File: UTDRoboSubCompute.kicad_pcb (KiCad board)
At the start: 4 copper layers, 100 x 100.1 mm, 52 parts, among them IC1 TPD4E05U06QDQARQ1, IC2 TPD4E05U06QDQARQ1, J1 Disable Bluetooth/Wifi, J10 HEADER-3X04, J11 HEADER-3X04, J12 HEADER-3X04, J13 Conn_02x20_Odd_Even, J14 GSB3116344KHHR, J15 GSB3116344KHHR, J16 TF38-22S-0.5SV_830_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

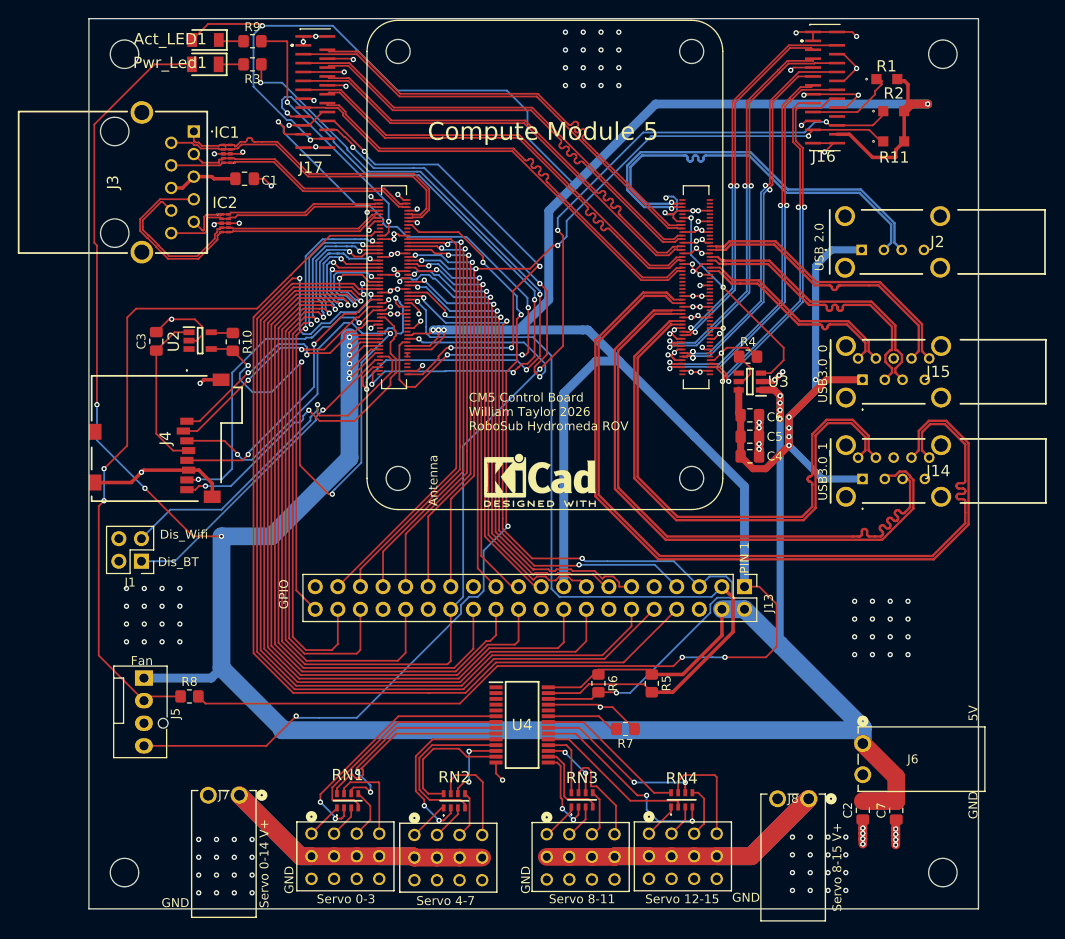
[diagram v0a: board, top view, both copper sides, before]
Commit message: Better trace spacing, JLCPCB compliant & misc fixes
 - Added JLCPCB rules file
 - Made design JLCPCB compliant
 - updated README.md with additional details about diff and non-diff trace routing
 - updated images in README.md
 - updated clearance specs for signaling lines to 3*W
 - flipped GPIO header and reflected spacing changes in routing
 - Fixed Servo Address register floating pins issue
 - Fixed 3.3v input on SD power IC non-connection
 - rerouted servo PWM lines for better spacing
 - rerouted SD card data lines for better spacing, and clearer routes
 - Switched Servo Power Traces to fills in order to allow for multi-layer connections
 - added extra pads for bulk capacitors
 - added more descriptive silkscreens
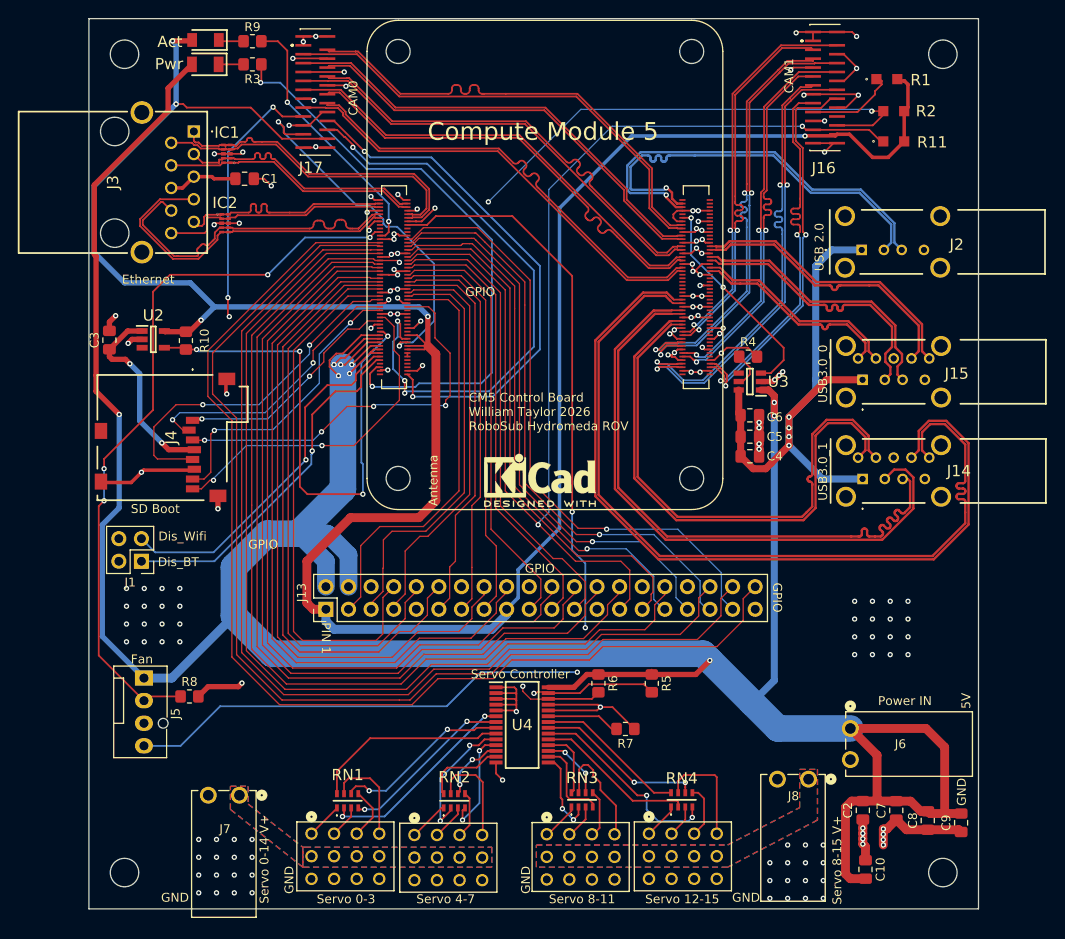
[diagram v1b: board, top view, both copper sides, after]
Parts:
- added C10: ~, Capacitor_SMD:C_0805_2012Metric_Pad1.18x1.45mm_HandSolder, F.Cu at (183.0, 150.8)
- added C8: ~, Capacitor_SMD:C_0805_2012Metric_Pad1.18x1.45mm_HandSolder, F.Cu at (190.0, 145.2)
- added C9: ~, Capacitor_SMD:C_0805_2012Metric_Pad1.18x1.45mm_HandSolder, F.Cu at (193.8, 145.5)
- moved J13 47.1 mm to (122.3, 121.5), turned to 90 degrees
- moved R10 5.27 mm to (106.6, 91.3)
- moved C3 5.27 mm to (98.0, 91.2)
- moved U2 5.27 mm to (102.9, 91.2)
- moved J8 2.20 mm to (176.6, 140.6)
- moved J6 2.20 mm to (181.3, 134.9)
- moved J4 0.65 mm to (105.1, 102.2)
- renumbered Act_LED1 to Act, Pwr_Led1 to Pwr
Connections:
- R10 pad 1: /+3.3v -> +3V3
- U2 pad 5: /+3.3v -> +3V3
- U4 pad 1: unconnected-(U4-A0-Pad1) -> GND
- U4 pad 2: unconnected-(U4-A1-Pad2) -> GND
- U4 pad 24: unconnected-(U4-A5-Pad24) -> GND
- U4 pad 3: unconnected-(U4-A2-Pad3) -> GND
- U4 pad 4: unconnected-(U4-A3-Pad4) -> GND
- U4 pad 5: unconnected-(U4-A4-Pad5) -> GND
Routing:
- net /GPIO21: track 50.9 -> 127.9 mm, vias 2 -> 0
- net /GPIO20: track 63.0 -> 123.2 mm, vias 2 -> 0
- net /GPIO14: track 115.6 -> 60.4 mm, vias 2 -> 0
- net +Servo 8-15 voltage: track 49.1 -> 0.00 mm
- net /GPIO16: track 67.3 -> 116.3 mm, vias 2 -> 0
- net +Servo 0-7 voltage: track 45.2 -> 0.00 mm
- net +5V: track 316.8 -> 359.2 mm, vias 13 -> 9
- net /GPIO15: track 103.2 -> 64.2 mm
- net /GPIO0: track 99.0 -> 137.6 mm, vias 4 -> 2
- net +3V3: track 328.1 -> 290.5 mm, vias 8 -> 6
- net /GPIO12: track 74.6 -> 109.5 mm, vias 2 -> 0
- net GND: track 211.0 -> 244.8 mm, vias 173 -> 157
- net /GPIO18: track 101.9 -> 68.7 mm, vias 2 -> 0
- net /SDA0: track 68.1 -> 41.2 mm, vias 4 -> 2
- net /GPIO23: track 102.1 -> 76.0 mm, vias 2 -> 0
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- added copper zone on B.Cu, net +Servo 0-7 voltage
- added copper zone on F.Cu, net +Servo 0-7 voltage
- added copper zone on In1.Cu, net +Servo 0-7 voltage
- added copper zone on In2.Cu, net +Servo 0-7 voltage
- added copper zone on B.Cu, net +Servo 8-15 voltage
- added copper zone on F.Cu, net +Servo 8-15 voltage
- added copper zone on In1.Cu, net +Servo 8-15 voltage
- added copper zone on In2.Cu, net +Servo 8-15 voltage
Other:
- board text added: "CAM0"
- board text added: "CAM1"
- board text added: "Ethernet"
- board text added: "Power IN"
- board text added: "SD Boot"
- board text added: "Servo Controller"

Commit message: Added and adjusted decoupling caps
- added decoupling capacitors to the USB IC
- corrected the value of the center tap decoupling capacitor
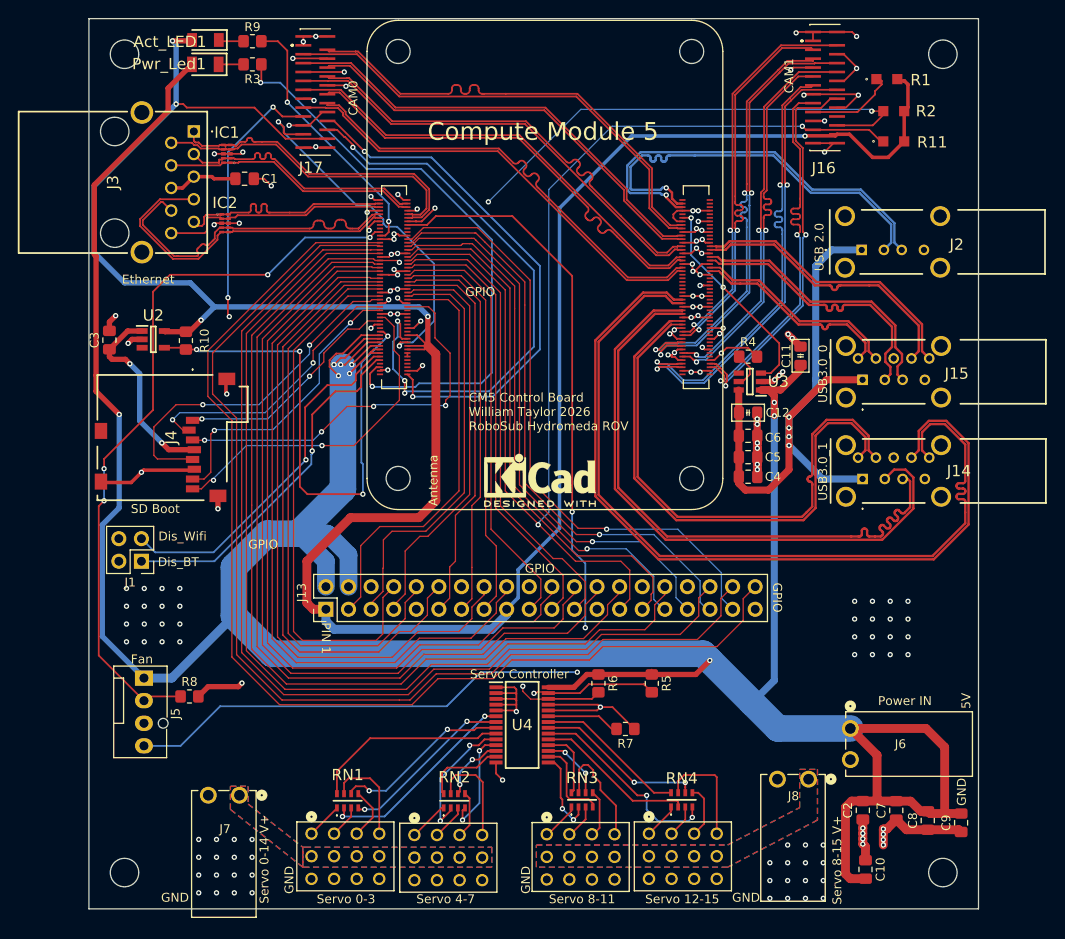
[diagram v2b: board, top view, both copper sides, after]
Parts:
- added C11: 0.1u, PCM_Capacitor_SMD_AKL:C_0805_2012Metric_Pad1.15x1.40mm_HandSolder, F.Cu at (175.7, 93.0)
- added C12: 0.1u, PCM_Capacitor_SMD_AKL:C_0805_2012Metric_Pad1.15x1.40mm_HandSolder, F.Cu at (169.8, 99.4)
- C1: value 100p -> 0.1u
- moved C5 2.31 mm to (169.8, 104.4)
- moved C4 2.31 mm to (169.8, 106.6)
- moved C6 2.31 mm to (169.8, 102.0)
- renumbered Act to Act_LED1, Pwr to Pwr_Led1
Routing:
- net +5V: track 359.2 -> 365.2 mm
- net /VBUS: track 65.0 -> 70.5 mm
- net GND: track 244.8 -> 249.4 mm, vias 157 -> 161

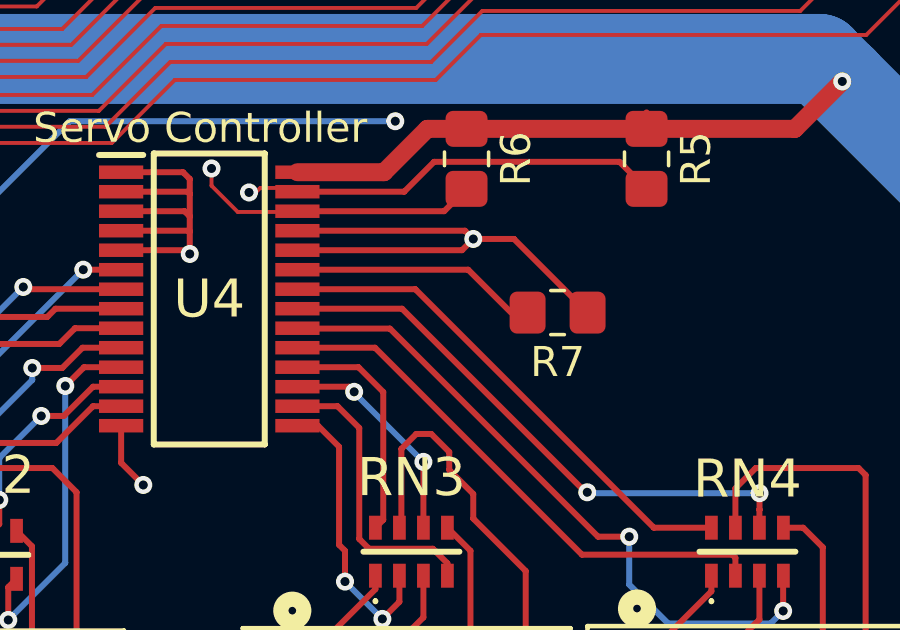
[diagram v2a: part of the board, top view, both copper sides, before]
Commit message: Removed unneeded pull down
Removed unnecessary pull down resistor on the OE pin of the Servo Controller. Since I am not folding out the output enable pin, a pull down is not needed
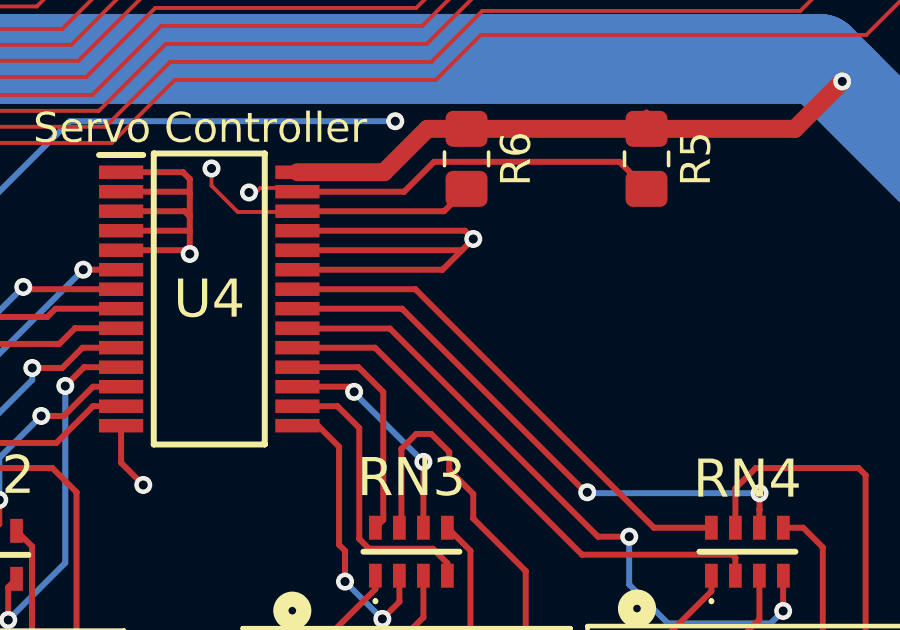
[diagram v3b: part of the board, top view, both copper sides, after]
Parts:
- removed R7: 10K, Resistor_SMD:R_0805_2012Metric_Pad1.20x1.40mm_HandSolder
- R10: value 10K -> 12K
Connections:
- U4 pad 23: Net-(U4-#OE) -> GND
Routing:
- net Net-(U4-#OE): track 7.72 -> 0.00 mm
- net GND: track 249.4 -> 250.4 mm

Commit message: Finished first verson
- updated bom
- added a more caps
- changed value of resistor according to data sheet
- updated ibom
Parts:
- renumbered Act_LED1 to Act1, Pwr_Led1 to Pwr1
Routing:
- net GND: track 250.4 -> 174.4 mm, vias 161 -> 180
- net /DPHY0_D1_P: track 48.8 -> 52.6 mm
- net /DPHY0_D1_N: track 51.4 -> 52.7 mm
- net /Act_LED: track 29.6 -> 30.8 mm
- net /DPHY0_D0_P: track 53.2 -> 54.2 mm
- net /DPHY0_D0_N: track 53.1 -> 54.1 mm
- net /Power_LED: track 67.5 -> 66.7 mm
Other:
- board text added: "CM5 Control Board William Taylor 2026 RoboSub Hydromeda ROV Version 1.0"
- board text added: "Docs"
- board text removed: "CM5 Control Board William Taylor 2026 RoboSub Hydromeda ROV"
